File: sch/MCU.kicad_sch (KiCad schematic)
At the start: 32 parts, among them J1 DE9_Pins_MountingHoles, J2 2x7P Pitch:1.27mm, SW1 TS-1087S-01526, U1 STM32G474CBT6, Y1 16MHz

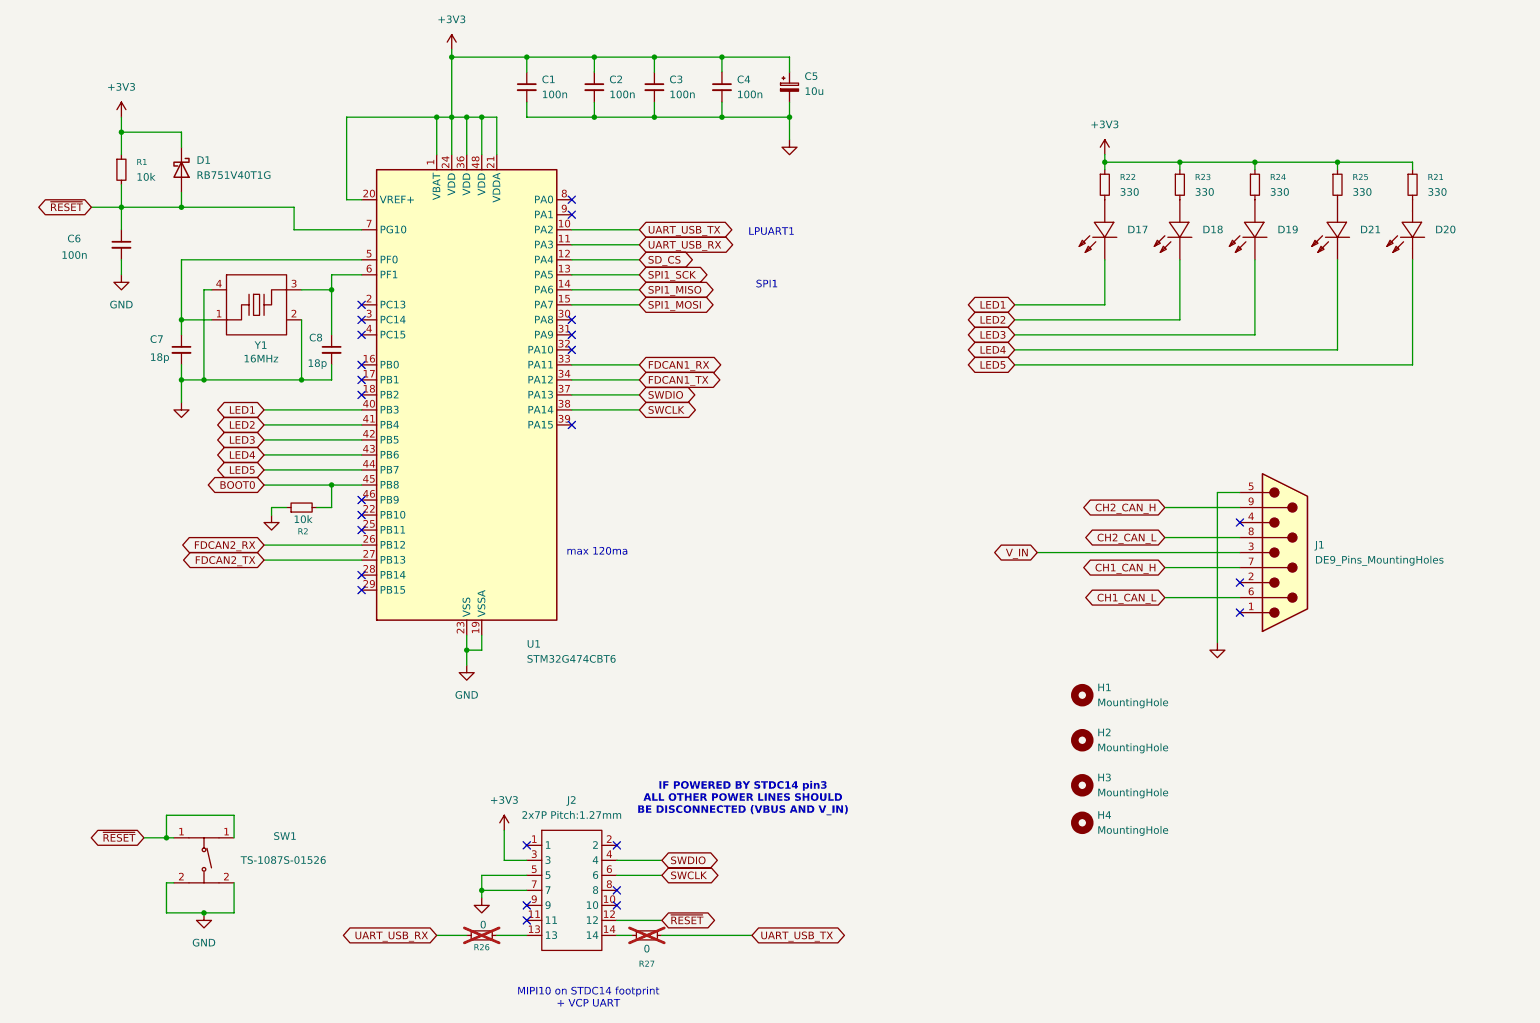
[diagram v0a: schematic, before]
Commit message: v1.1 changes * increase LED resistors as they are too bright * replace solder jumpers with pins * add corresponding 3D models
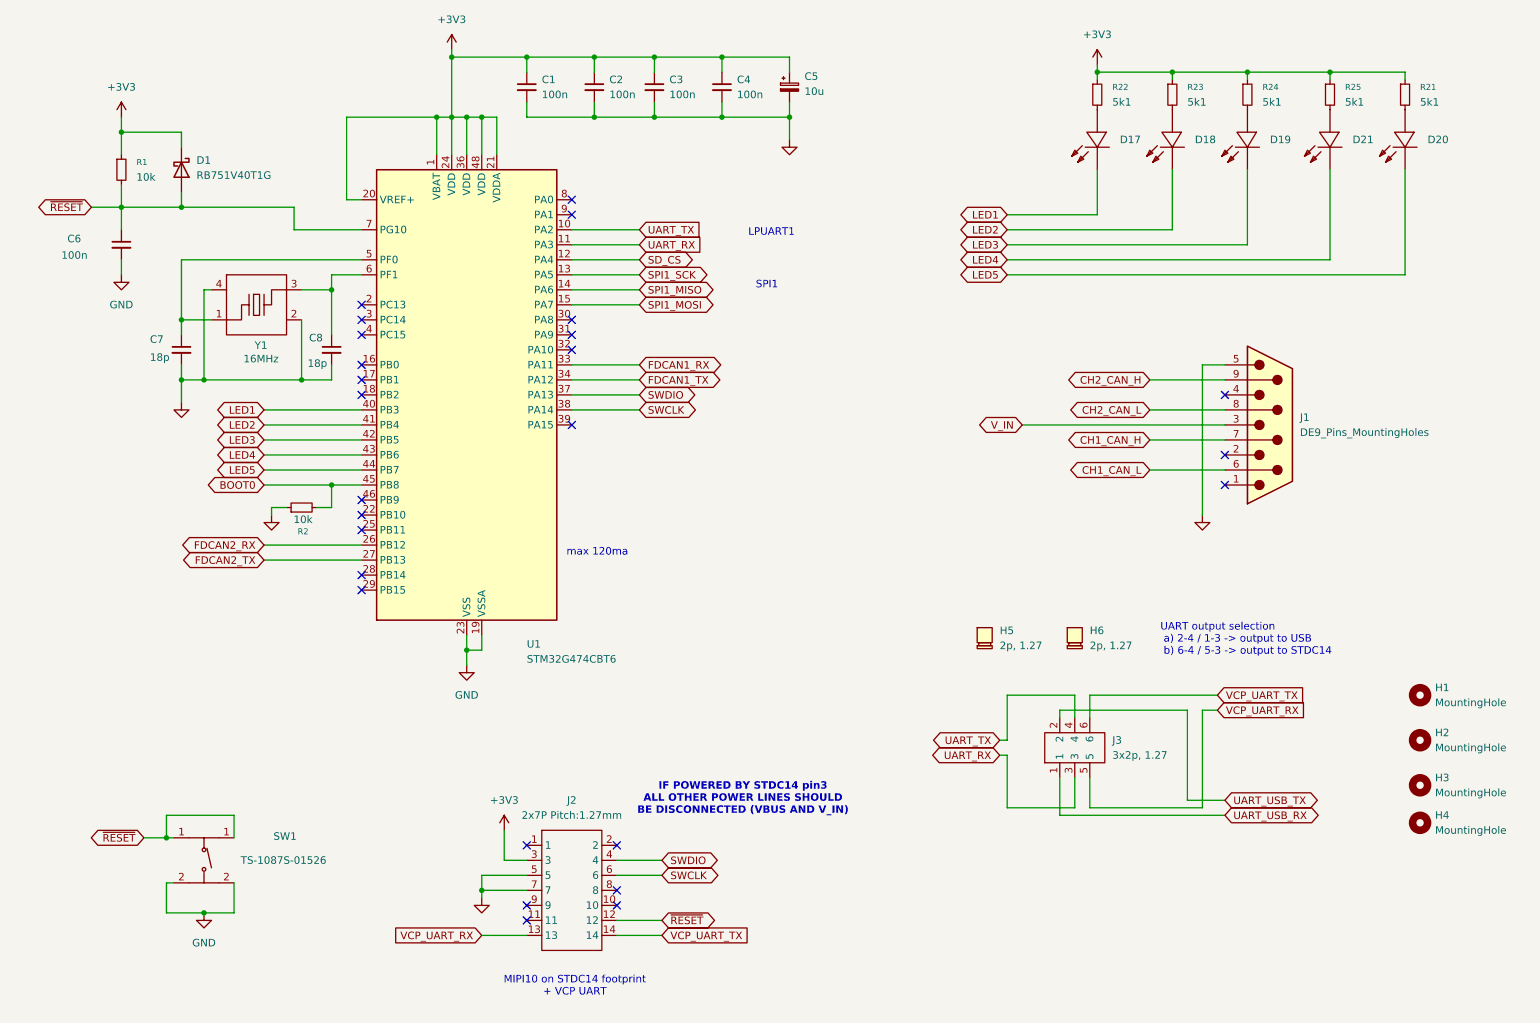
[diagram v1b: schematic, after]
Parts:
- removed R26, R27: 0, EasyEDA_Lib:R0603, symbol Device:R_Small
- added H5, H6: 2p, 1.27, symbol canlogger_custom_lib:Jumper_Shunt
- added J3: 3x2p, 1.27, canlogger_custom_lib:HDR-SMD_6P-P1.27-V-M-R2-C3-S1.27-LS5.5-1, symbol EasyEDA_Lib:DZ127S-22-06-55
- R21, R22, R23, R24, R25: value 330 -> 5k1; Supplier Part C23138 -> C23186
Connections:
- net UART_USB_RX: now also J3.1; no longer U1.11 (PA3)
- net UART_USB_TX: now also J3.2; no longer U1.10 (PA2)
- net VCP_UART_TX: now reaches J2.14
- net VCP_UART_TX: now also J3.6
- net VCP_UART_RX: now reaches J2.13
- net VCP_UART_RX: now also J3.5
- new net UART_RX: J3.3, U1.11 (PA3)
- new net UART_TX: J3.4, U1.10 (PA2)
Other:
- note added: "UART output selection a) 2-4 / 1-3 -> output to USB b) 6-4 / 5-3 -> output to STDC14"
- title: 2CH CAN  Logger -> Dual Channel CAN Logger
- moved on the sheet: D17, D18, D19, D20, D21, H1, H2, H3, H4, J1, R21, R22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
